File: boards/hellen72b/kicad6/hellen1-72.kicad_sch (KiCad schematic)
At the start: 41 parts

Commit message: update exported kicad files after refactoring
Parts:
- C1, C2, C3, C4, C5, J1, J2, J3, M1, M10, M11, M2, M3, M4, M5, M6, M7, M8, M9, P1, P2, P3, R1, R10, R11, R12, R2, R25, R26, R3, R4, R5, R6, R7, R8, R9, S1, S2, U1, U2: value (none) -> ~
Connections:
- net BOOT0: now also M2.N28 (BOOT0); no longer M2.N26 (BOOT0)
- net EXT_IO1: now also M2.N8 (SPI3_CS); no longer M2.N6 (IO1)
- net EXT_IO2: now also M2.N9 (SPI3_SCK); no longer M2.N7 (IO2)
- net EXT_IO3: now also M2.N10 (SPI3_MISO); no longer M2.N8 (IO3)
- net EXT_IO4: now also M2.N11 (SPI3_MOSI); no longer M2.N9 (IO4)
- net EXT_SPI_CS1: now also M2.E4 (SPI1_CS1); no longer M2.E4 (SPI_CS1)
- net EXT_SPI_CS2: now also M2.E5 (SPI1_CS2); no longer M2.E5 (SPI_CS2)
- net EXT_SPI_MISO: now also M2.E2 (SPI1_MISO); no longer M2.E2 (SPI_MISO)
- net EXT_SPI_MOSI: now also M2.E3 (SPI1_MOSI); no longer M2.E3 (SPI_MOSI)
- net EXT_SPI_SCK: now also M2.E1 (SPI1_SCK); no longer M2.E1 (SPI_SCK)
- net GND: now also M2.S2 (GND); no longer M1.E5 (GND), M2.S2 (GND), M4.V3 (GND)
- net GNDA: now also M1.J2 (PULL_GNDA), M1.N2 (GNDA), M2.S32 (GNDA); no longer M1.J2 (GNDA), M1.N2 (GNDA), M2.S32 (GNDA)
- net IGN1: now also M2.W1 (OUT_IGN1); no longer M2.W1 (OUT_IGN1)
- net IGN2: now also M2.W2 (OUT_IGN2); no longer M2.W2 (OUT_IGN2)
- net IGN3: now also M2.W3 (OUT_IGN3); no longer M2.W3 (OUT_IGN3)
- net IGN4: now also M2.W4 (OUT_IGN4); no longer M2.W4 (OUT_IGN4)
- net IGN5: now also M2.W5 (OUT_IGN5); no longer M2.W5 (OUT_IGN5)
- net IGN6: now also M2.W6 (OUT_IGN6); no longer M2.W6 (OUT_IGN6)
- net IGN7: now also M2.W7 (OUT_IGN7); no longer M2.W7 (OUT_IGN7)
- net IGN8: now also M2.W8 (OUT_IGN8); no longer M2.W8 (OUT_IGN8)
- net OUT_AC: now also M7.S12 (OUT_LOW6_PULLUP); no longer M7.S12 (OUT_LOW6_PULLUP)
- net OUT_COIL_A1: now also M7.S1 (OUT_SOLENOID_A1); no longer M7.S1 (OUT_COIL_A1)
- net OUT_COIL_A2: now also M7.S2 (OUT_SOLENOID_A2); no longer M7.S2 (OUT_COIL_A2)
- net OUT_COIL_B1: now also M7.S4 (OUT_SOLENOID_B1); no longer M7.S4 (OUT_COIL_B1)
- net OUT_COIL_B2: now also M7.S5 (OUT_SOLENOID_B2); no longer M7.S5 (OUT_COIL_B2)
- net OUT_ECF: now also M7.S8 (OUT_LOW8); no longer M7.S8 (OUT_LOW8)
- net OUT_IDLE: now also M7.S10 (OUT_LOW10); no longer M7.S10 (OUT_LOW10)
- net OUT_INJ1: now also M7.S18 (OUT_INJ1); no longer M7.S18 (OUT_INJ1)
- net OUT_INJ2: now also M7.S16 (OUT_INJ2); no longer M7.S16 (OUT_INJ2)
- net OUT_INJ3: now also M7.S17 (OUT_INJ3); no longer M7.S17 (OUT_INJ3)
- net OUT_INJ6: now also M7.S15 (OUT_INJ6); no longer M7.S15 (OUT_INJ6)
- net OUT_O2H: now also M7.S7 (OUT_LOW1_DUAL); no longer M7.S7 (OUT_LOW1_DUAL)
- net OUT_PUMP: now also M7.S14 (OUT_LOW7); no longer M7.S14 (OUT_LOW7)
- net OUT_TACH: now also M7.S6 (OUT_PP2); no longer M7.S6 (OUT_PP2)
- net OUT_VVT: now also M7.S13 (OUT_LOW11); no longer M7.S13 (OUT_LOW11)
- net SD_CS: now also M2.N23 (SPI2_CS); no longer M2.N21 (SD_CS)
- net SD_MISO: now also M2.N21 (SPI2_MISO); no longer M2.N19 (SD_MISO)
- net SD_MOSI: now also M2.N22 (SPI2_MOSI); no longer M2.N20 (SD_MOSI)
- net SD_SCK: now also M2.N20 (SPI2_SCK); no longer M2.N18 (SD_SCK)
- net SWCLK: now also M2.N25 (SWCLK); no longer M2.N23 (SWCLK)
- net SWDIO: now also M2.N26 (SWDIO); no longer M2.N24 (SWDIO)
- net SWO: now also M2.N27 (SWO); no longer M2.N25 (SWO)
- net UART_RX: now also M2.N7 (UART2_RX); no longer M2.N5 (UART_RX)
- net UART_TX: now also M2.N6 (UART2_TX); no longer M2.N4 (UART_TX)
- net USB_N: now also M2.N31 (USB1M); no longer M2.N29 (USBM)
- net USB_P: now also M2.N30 (USB1P); no longer M2.N28 (USBP)
- net V12P: now also M7.W5 (V12P); no longer M7.W5 (V12P)
- net V33: now also M2.N16 (V33); no longer M2.N14 (V33)
- net V5: now also M2.S1 (V5), M7.W14 (V5); no longer M2.S1 (V5), M7.W14 (V5)
- net V5A: now also M1.J1 (PULL_V5A), M1.N1 (V5A), M2.S33 (V5A); no longer M1.E6 (V5A), M1.J1 (V5A), M1.N1 (V5A), M2.S33 (V5A)
- net VBAT: now also M2.N17 (VBAT); no longer M2.N15 (VBAT)
- net VBUS: now also M2.N29 (VBUS); no longer C2.2, M2.N27 (VBUS)
- net VREF2: now also M1.S13 (VREF2); no longer M1.S13 (VREF2)
- net nReset: now also M2.N24 (nReset); no longer M2.N22 (nReset)
- no-connect marks 39 -> 41

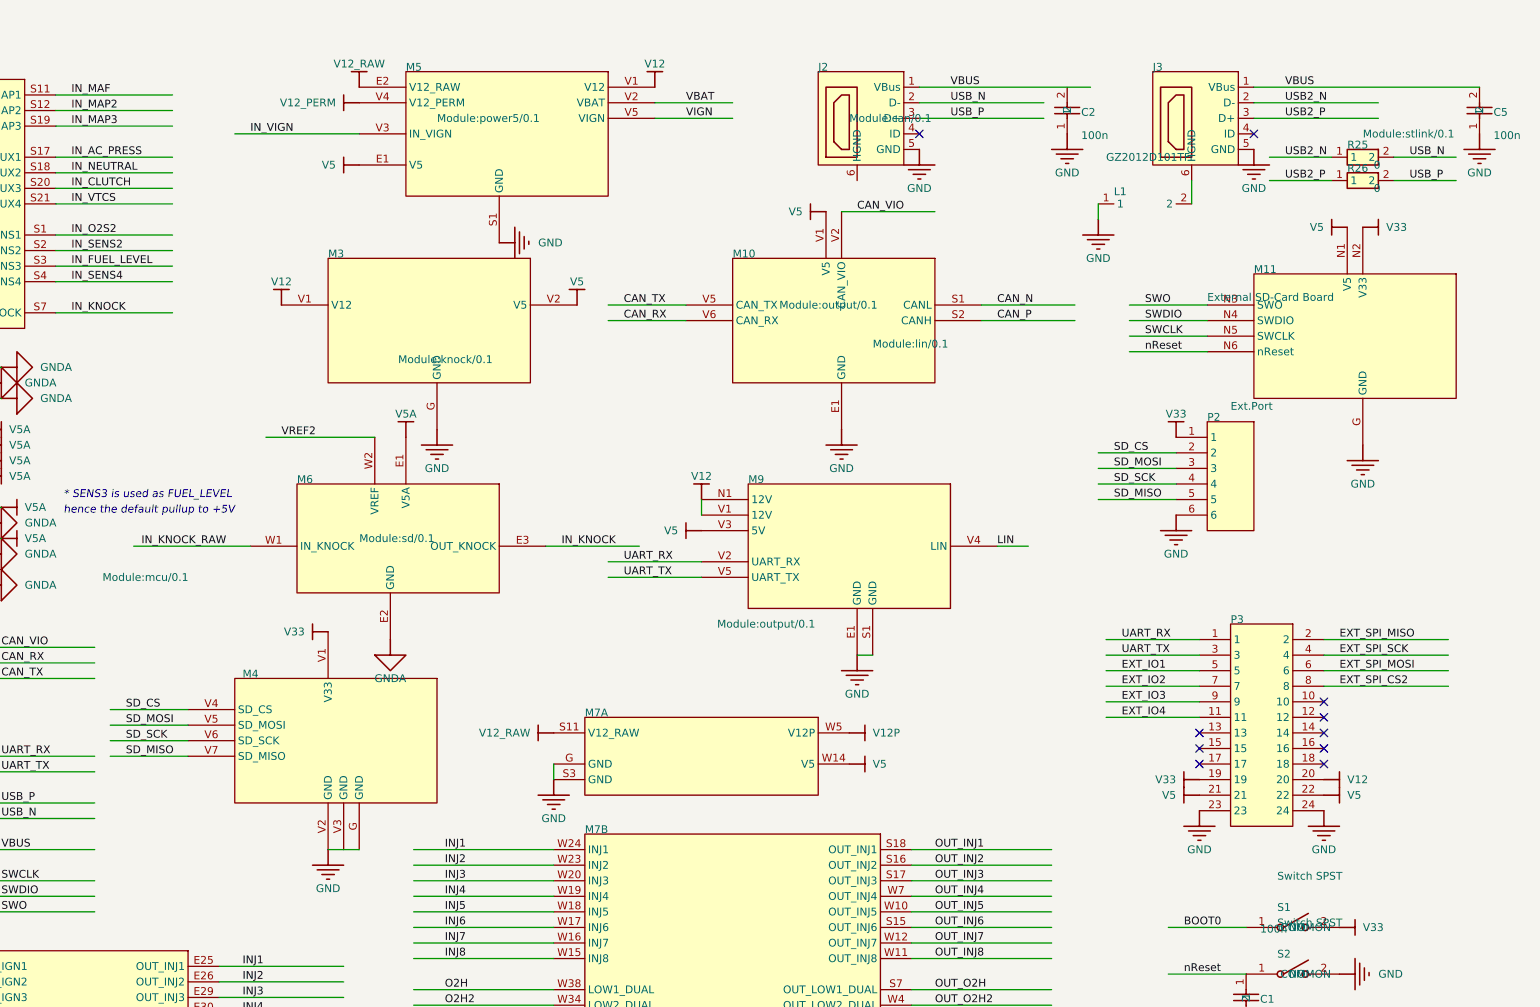
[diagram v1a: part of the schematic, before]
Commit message: update after refactoring can,lin,sd,stlink
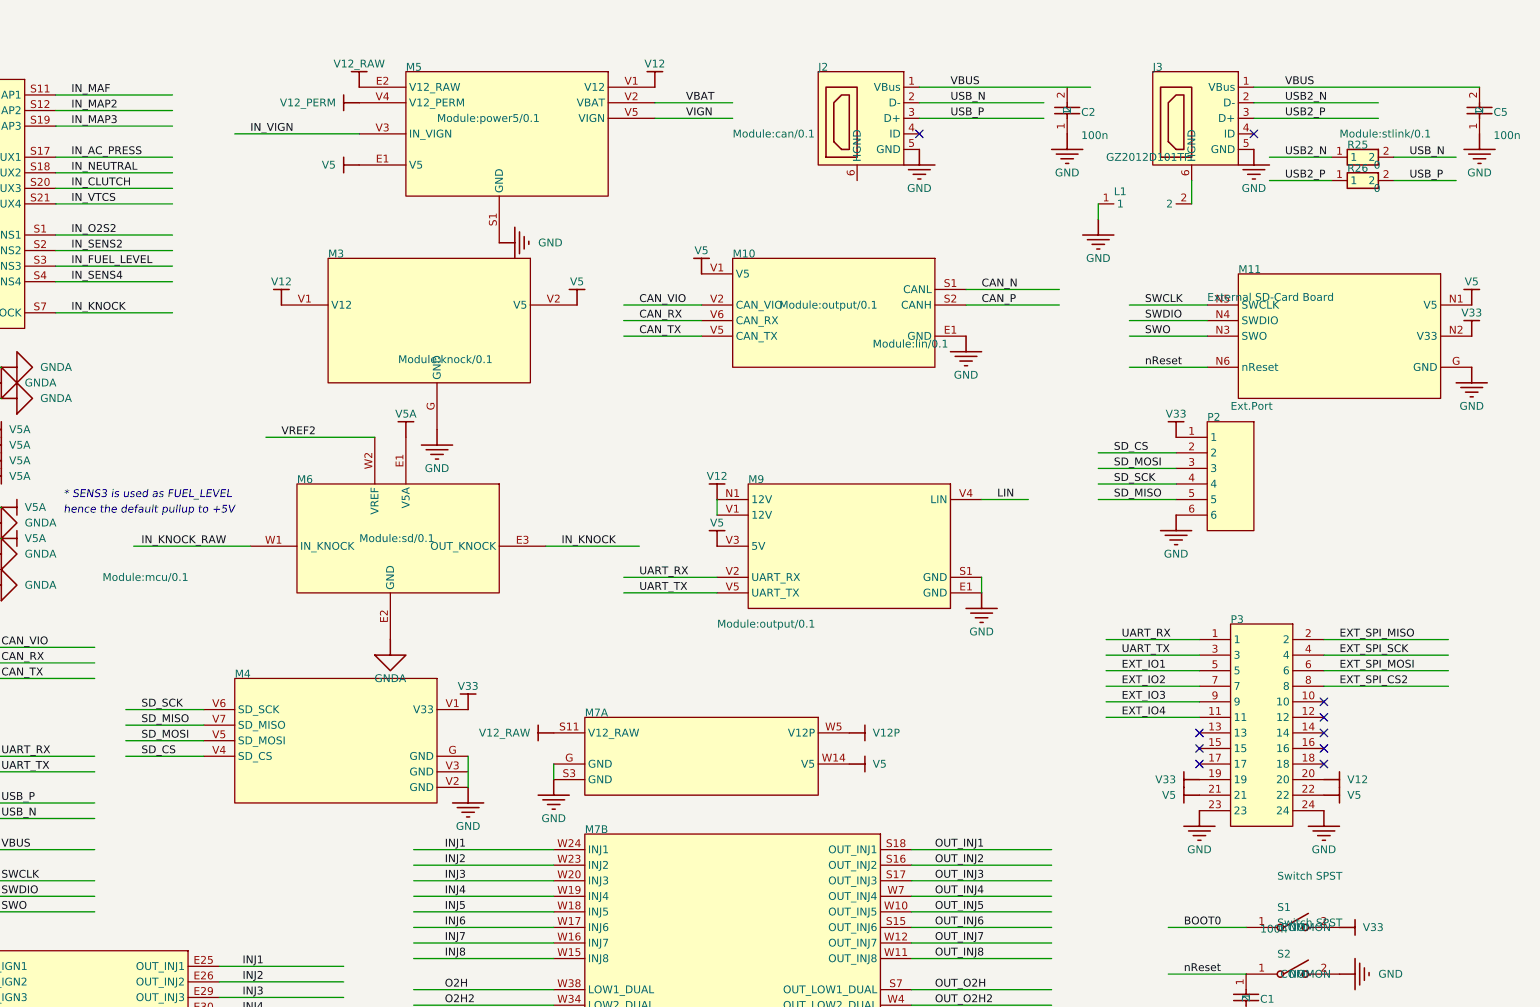
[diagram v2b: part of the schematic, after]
